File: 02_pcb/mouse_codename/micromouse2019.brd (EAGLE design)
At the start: 45 x 50 mm, 78 parts

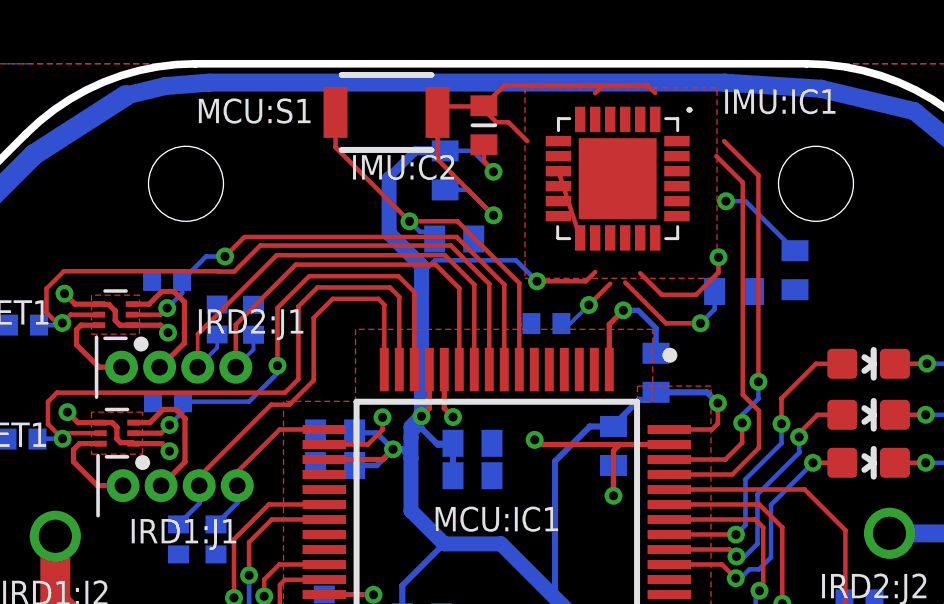
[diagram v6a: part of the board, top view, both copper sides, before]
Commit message: mpu6050 board layout fix
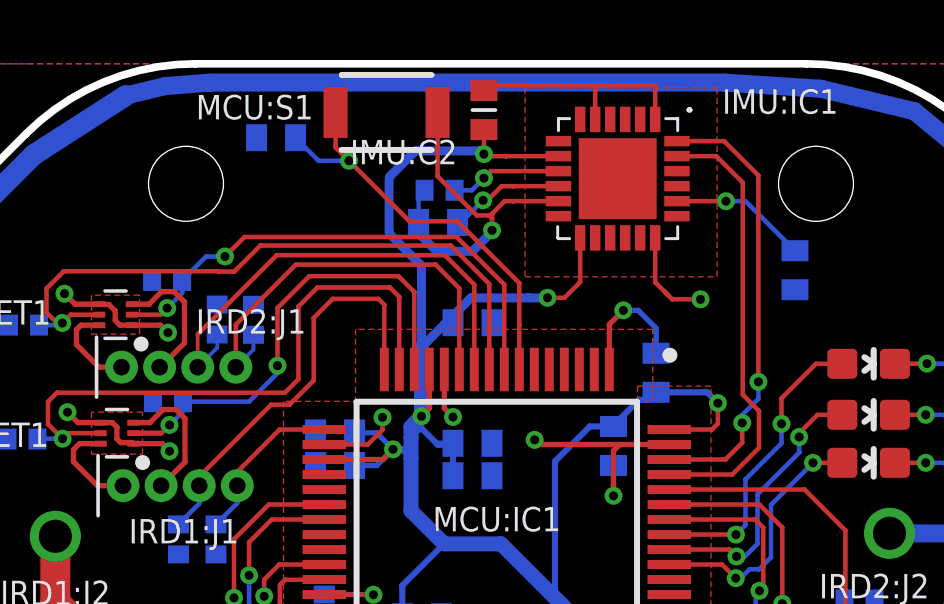
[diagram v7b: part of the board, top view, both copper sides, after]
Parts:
- moved IMU:C1 10.1 mm to (20.4, 44.7), turned to 0 degrees
- moved MCU:C11 6.83 mm to (15.0, 47.5), turned to 0 degrees
- moved IMU:R1 5.69 mm to (20.5, 45.8)
- moved IMU:C4 5.16 mm to (21.6, 41.4), turned to 180 degrees
- moved IMU:C2 0.51 mm to (21.9, 48.5)
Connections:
- net GND: no longer IMU:IC1.15
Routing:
- net GND: track 112.0 -> 115.5 mm
- net IMU:CPOUT: track 2.99 -> 4.62 mm
- net SDA: track 13.4 -> 15.0 mm
- net IMU:AD0: track 2.18 -> 3.72 mm
- net SCL: track 13.7 -> 15.0 mm
- net +3V3: track 165.7 -> 167.0 mm
- net MCU:NRST: track 13.1 -> 14.1 mm

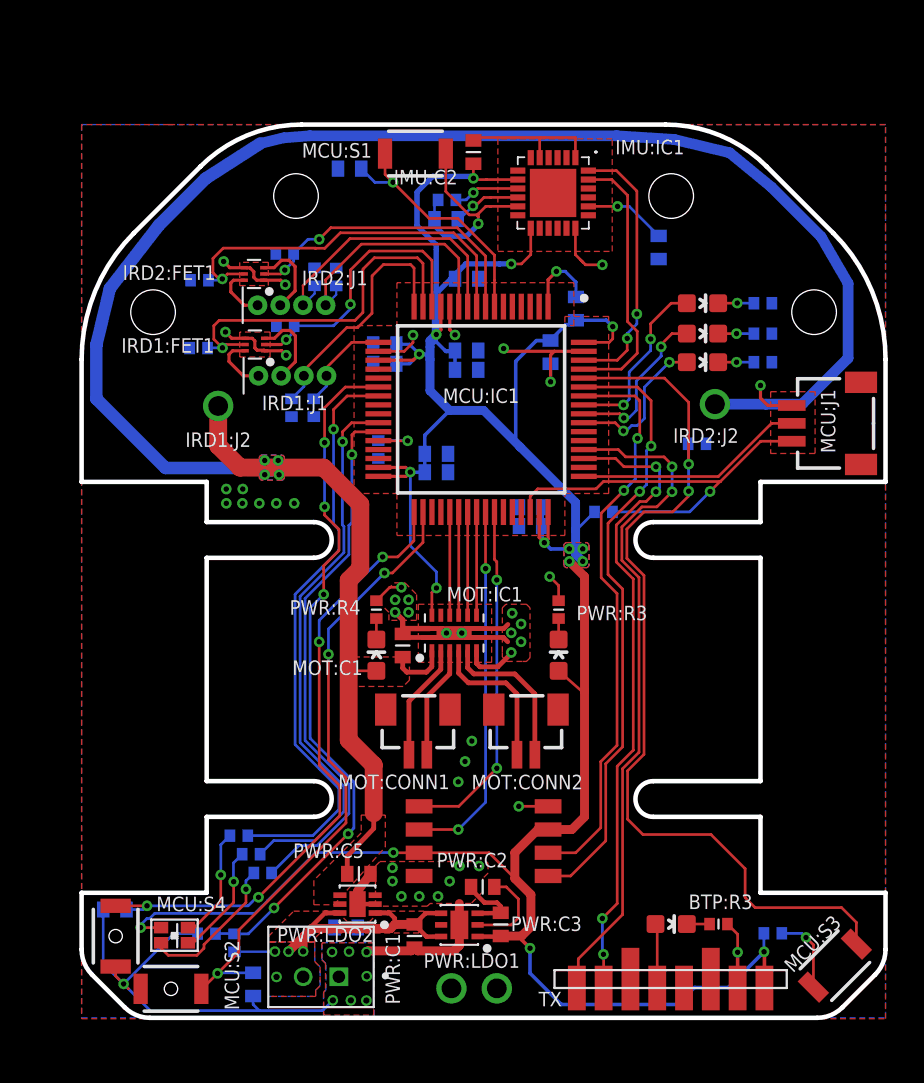
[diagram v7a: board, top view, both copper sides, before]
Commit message: board updated, strange polygon clearances
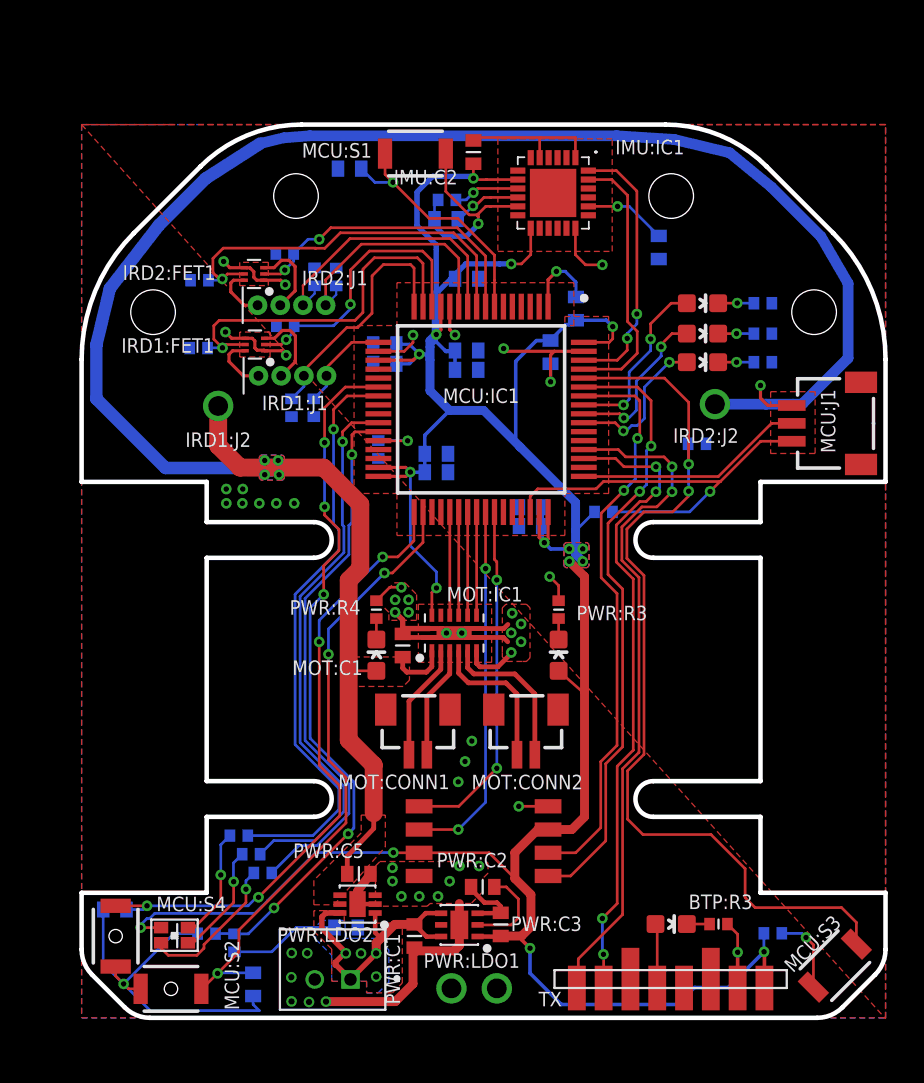
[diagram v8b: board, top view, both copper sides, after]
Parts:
- moved PWR:CONN1 0.67 mm to (14.1, 2.70)
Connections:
- net GND: now also PWR:CONN1.2; no longer PWR:CONN1.1
- net PWR:V_BAT_IN: now also PWR:CONN1.1; no longer PWR:CONN1.2
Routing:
- net PWR:V_BAT_IN: track 20.6 -> 22.3 mm
- net GND: track 115.5 -> 116.2 mm, vias 52 -> 51
